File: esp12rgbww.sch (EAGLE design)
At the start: 16 parts, among them J1 1X2-3.5MM, J2 1X2-3.5MM, J3 1X2-3.5MM

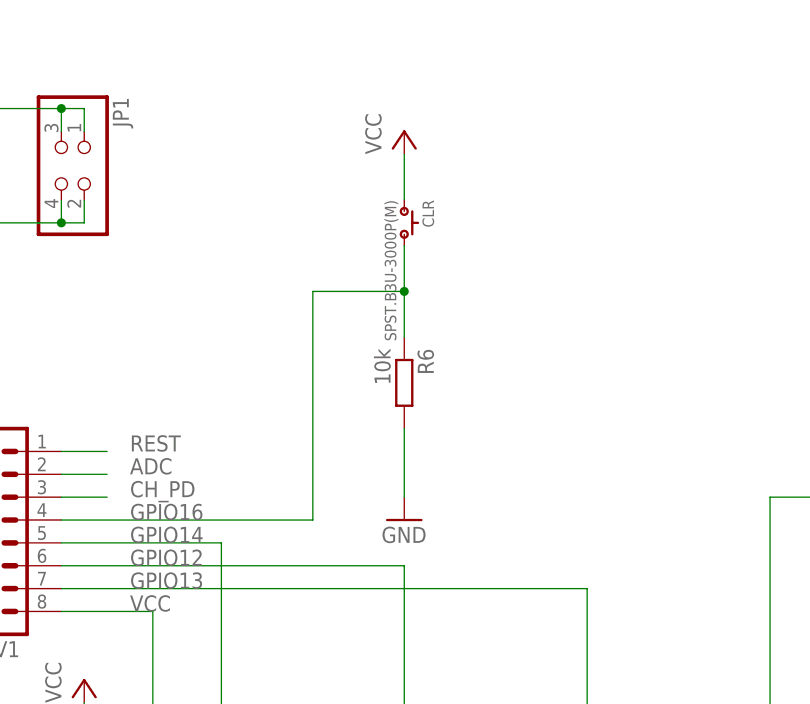
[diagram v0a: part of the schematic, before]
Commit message: FT232 module
FT232 Module now functional as a prototype
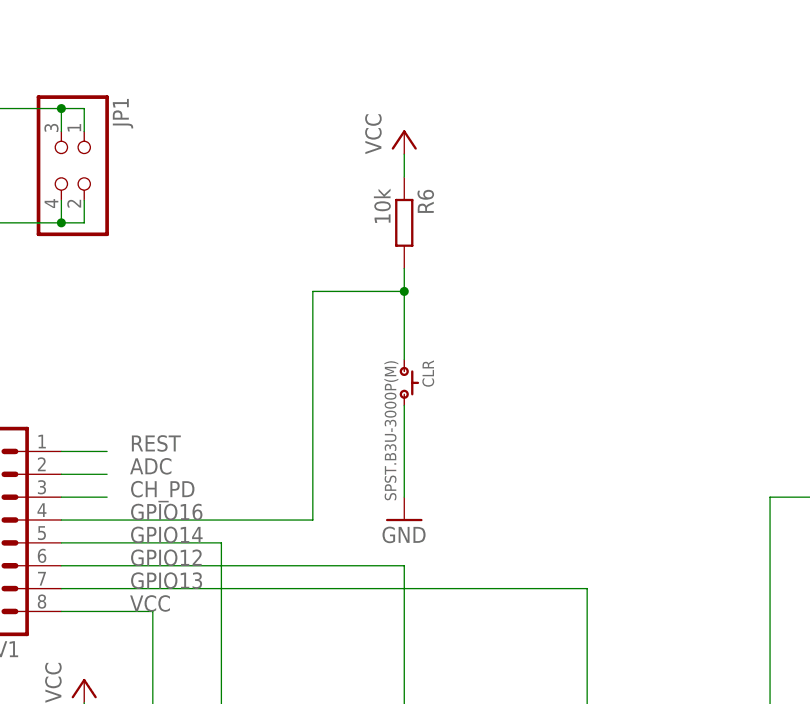
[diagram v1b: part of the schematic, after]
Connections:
- net GND: now also CLR.2; no longer R6.2
- net GPIO16: now also CLR.1, R6.2; no longer CLR.2, R6.1
- net VCC: now also R6.1; no longer CLR.1
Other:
- moved on the sheet: CLR, R6
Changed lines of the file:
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@@
 <instance part="J2" gate="G$1" x="63.5" y="-53.34" rot="R270"/>
 <instance part="J3" gate="G$1" x="71.12" y="-53.34" rot="R270"/>
-<instance part="R6" gate="G$1" x="68.58" y="50.8" rot="R270"/>
+<instance part="R6" gate="G$1" x="68.58" y="68.58" rot="R270"/>
 <instance part="GND3" gate="1" x="147.32" y="15.24"/>
 <instance part="P+2" gate="VCC" x="33.02" y="17.78"/>
 <instance part="GND4" gate="1" x="68.58" y="35.56"/>
 <instance part="P+4" gate="VCC" x="68.58" y="78.74"/>
-<instance part="CLR" gate="G$1" x="68.58" y="68.58" rot="R270"/>
+<instance part="CLR" gate="G$1" x="68.58" y="50.8" rot="R270"/>
 </instances>
 <busses>
@@
 </segment>
 <segment>
-<pinref part="R6" gate="G$1" pin="2"/>
+<pinref part="CLR" gate="G$1" pin="2"/>
 <pinref part="GND4" gate="1" pin="GND"/>
-<wire x1="68.58" y1="45.72" x2="68.58" y2="38.1" width="0.1524" layer="91"/>
+<wire x1="68.58" y1="48.26" x2="68.58" y2="38.1" width="0.1524" layer="91"/>
 </segment>
 </net>
@@
 </segment>
 <segment>
-<pinref part="CLR" gate="G$1" pin="1"/>
 <pinref part="P+4" gate="VCC" pin="VCC"/>
-<wire x1="68.58" y1="71.12" x2="68.58" y2="76.2" width="0.1524" layer="91"/>
+<pinref part="R6" gate="G$1" pin="1"/>
+<wire x1="68.58" y1="76.2" x2="68.58" y2="73.66" width="0.1524" layer="91"/>
 </segment>
 </net>
@@
 <pinref part="SV1" gate="1" pin="4"/>
 <label x="38.1" y="35.56" size="1.778" layer="95"/>
-<pinref part="R6" gate="G$1" pin="1"/>
-<wire x1="68.58" y1="55.88" x2="68.58" y2="60.96" width="0.1524" layer="91"/>
 <wire x1="68.58" y1="60.96" x2="58.42" y2="60.96" width="0.1524" layer="91"/>
 <wire x1="58.42" y1="60.96" x2="58.42" y2="35.56" width="0.1524" layer="91"/>
 <wire x1="58.42" y1="35.56" x2="30.48" y2="35.56" width="0.1524" layer="91"/>
-<pinref part="CLR" gate="G$1" pin="2"/>
-<wire x1="68.58" y1="66.04" x2="68.58" y2="60.96" width="0.1524" layer="91"/>
+<pinref part="R6" gate="G$1" pin="2"/>
+<wire x1="68.58" y1="63.5" x2="68.58" y2="60.96" width="0.1524" layer="91"/>
+<pinref part="CLR" gate="G$1" pin="1"/>
+<wire x1="68.58" y1="60.96" x2="68.58" y2="53.34" width="0.1524" layer="91"/>
 <junction x="68.58" y="60.96"/>
 </segment>
